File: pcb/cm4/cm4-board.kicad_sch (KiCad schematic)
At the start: 11 parts, among them J201 DF40C-100DS-0.4V_51_, J202 DF40C-100DS-0.4V_51_, U201 SN74LV1T34DBV

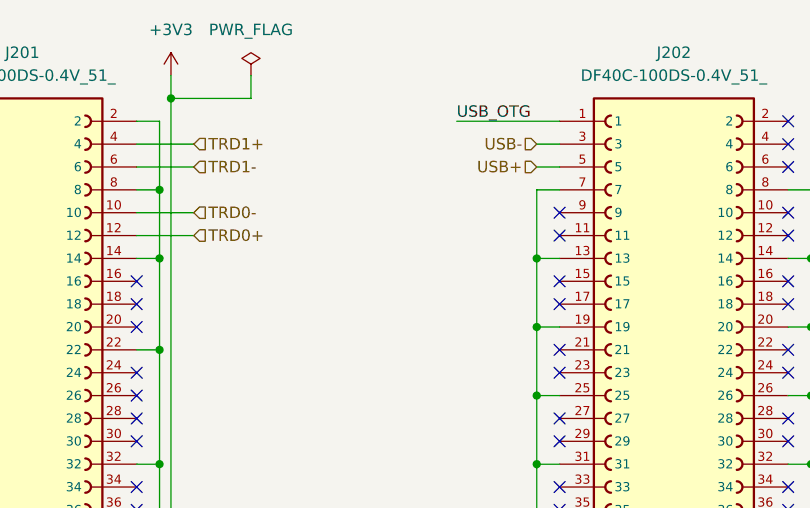
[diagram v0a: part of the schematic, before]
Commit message: add more caps
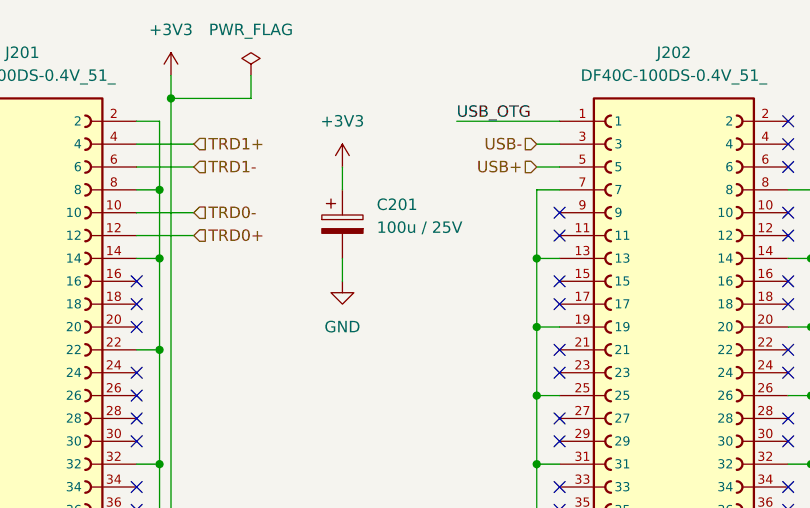
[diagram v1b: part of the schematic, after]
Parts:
- added C201: 100u / 25V, Capacitor_Tantalum_SMD:CP_EIA-7343-43_Kemet-X_Pad2.25x2.55mm_HandSolder, symbol Device:C_Polarized
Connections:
- net +3V3: now also C201.1
- net GND: now also C201.2
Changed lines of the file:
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@@
+	(wire
+		(pts
+			(xy 101.6 36.83) (xy 101.6 39.37)
+		)
+		(stroke
+			(width 0)
+			(type default)
+		)
+	)
 	(wire
 		(pts
@@
 		(pts
 			(xy 50.8 105.41) (xy 53.34 105.41)
+		)
+		(stroke
+			(width 0)
+			(type default)
+		)
+	)
+	(wire
+		(pts
+			(xy 101.6 46.99) (xy 101.6 49.53)
 		)
 		(stroke
@@
 	)
 	(symbol
+		(lib_id "power:GND")
+		(at 101.6 49.53 0)
+		(unit 1)
+		(exclude_from_sim no)
+		(in_bom yes)
+		(on_board yes)
+		(dnp no)
+		(fields_autoplaced yes)
+		(property "Reference" "#PWR0215"
+			(at 101.6 55.88 0)
+			(effects
+				(font
+					(size 1.27 1.27)
+				)
+				(hide yes)
+			)
+		)
+		(property "Value" "GND"
+			(at 101.6 54.61 0)
+			(effects
+				(font
+					(size 1.27 1.27)
+				)
+			)
+		)
+		(property "Footprint" ""
+			(at 101.6 49.53 0)
+			(effects
+				(font
+					(size 1.27 1.27)
+				)
+				(hide yes)
+			)
+		)
+		(property "Datasheet" ""
+			(at 101.6 49.53 0)
+			(effects
+				(font
+					(size 1.27 1.27)
+				)
+				(hide yes)
+			)
+		)
+		(property "Description" "Power symbol creates a global label with name \"GND\" , ground"
+			(at 101.6 49.53 0)
+			(effects
+				(font
+					(size 1.27 1.27)
+				)
+				(hide yes)
+			)
+		)
+		(pin "1"
+		)
+		(instances
+			(project "cm4"
+				(path "/5d20b266-567e-45c6-9e3e-145c2aea1daa/a64f9485-8eaf-45a8-a9d7-21ab5cb8dcb2"
+					(reference "#PWR0215")
+					(unit 1)
+				)
+			)
+		)
+	)
+	(symbol
 		(lib_id "power:+3V3")
 		(at 256.54 107.95 0)
@@
 					(unit 1)
 				)
+			)
+		)
+	)
+	(symbol
+		(lib_id "power:+3V3")
+		(at 101.6 36.83 0)
+		(unit 1)
+		(exclude_from_sim no)
+		(in_bom yes)
+		(on_board yes)
+		(dnp no)
+		(fields_autoplaced yes)
+		(property "Reference" "#PWR0214"
+			(at 101.6 40.64 0)
+			(effects
+				(font
+					(size 1.27 1.27)
+				)
+				(hide yes)
+			)
+		)
+		(property "Value" "+3V3"
+			(at 101.6 31.75 0)
+			(effects
+				(font
+					(size 1.27 1.27)
+				)
+			)
+		)
+		(property "Footprint" ""
+			(at 101.6 36.83 0)
+			(effects
+				(font
+					(size 1.27 1.27)
+				)
+				(hide yes)
+			)
+		)
+		(property "Datasheet" ""
+			(at 101.6 36.83 0)
+			(effects
+				(font
+					(size 1.27 1.27)
+				)
+				(hide yes)
+			)
+		)
+		(property "Description" "Power symbol creates a global label with name \"+3V3\""
+			(at 101.6 36.83 0)
+			(effects
+				(font
+					(size 1.27 1.27)
+				)
+				(hide yes)
+			)
+		)
+		(pin "1"
+		)
+		(instances
+			(project "cm4"
+				(path "/5d20b266-567e-45c6-9e3e-145c2aea1daa/a64f9485-8eaf-45a8-a9d7-21ab5cb8dcb2"
+					(reference "#PWR0214")
+					(unit 1)
+				)
+			)
+		)
+	)
+	(symbol
+		(lib_id "Device:C_Polarized")
+		(at 101.6 43.18 0)
+		(unit 1)
+		(exclude_from_sim no)
+		(in_bom yes)
+		(on_board yes)
+		(dnp no)
+		(fields_autoplaced yes)
+		(property "Reference" "C201"
+			(at 105.41 41.0209 0)
+			(effects
+				(font
+					(size 1.27 1.27)
+				)
+				(justify left)
+			)
+		)
+		(property "Value" "100u / 25V"
+			(at 105.41 43.5609 0)
+			(effects
+				(font
+					(size 1.27 1.27)
+				)
+				(justify left)
+			)
+		)
+		(property "Footprint" "Capacitor_Tantalum_SMD:CP_EIA-7343-43_Kemet-X_Pad2.25x2.55mm_HandSolder"
+			(at 102.5652 46.99 0)
+			(effects
+				(font
+					(size 1.27 1.27)
+				)
+				(hide yes)
+			)
+		)
+		(property "Datasheet" "~"
+			(at 101.6 43.18 0)
+			(effects
+				(font
+					(size 1.27 1.27)
+				)
+				(hide yes)
+			)
+		)
+		(property "Description" "Polarized capacitor"
+			(at 101.6 43.18 0)
+			(effects
+				(font
+					(size 1.27 1.27)
+				)
+				(hide yes)
+			)
+		)
+		(property "LCSC" "C7230"
+			(at 101.6 43.18 0)
+			(effects
+				(font
+					(size 1.27 1.27)
+				)
+				(hide yes)
+			)
+		)
+		(pin "2"
+		)
+		(pin "1"
+		)
+		(instances
+			(project "cm4"
+				(path "/5d20b266-567e-45c6-9e3e-145c2aea1daa/a64f9485-8eaf-45a8-a9d7-21ab5cb8dcb2"
+					(reference "C201")
+					(unit 1)
+				)

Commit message: update lscs fields
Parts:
- D201, D202: LCSC (none) -> C84256
- R201, R204: LCSC (none) -> C17513
- R202, R203, R205, R206: LCSC (none) -> C17520
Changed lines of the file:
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@@
 			)
 		)
-		(property "LCSC" ""
+		(property "LCSC" "C17513"
 			(at 256.54 124.46 0)
 			(effects
@@
 			)
 		)
-		(property "LCSC" ""
+		(property "LCSC" "C17520"
 			(at 224.79 66.04 0)
 			(effects
@@
 			)
 		)
-		(property "LCSC" ""
+		(property "LCSC" "C84256"
 			(at 199.39 118.11 0)
 			(effects
@@
 			)
 		)
-		(property "LCSC" ""
+		(property "LCSC" "C17520"
 			(at 177.8 64.77 0)
 			(effects
@@
 			)
 		)
-		(property "LCSC" ""
+		(property "LCSC" "C17520"
 			(at 190.5 64.77 0)
 			(effects
@@
 			)
 		)
-		(property "LCSC" ""
+		(property "LCSC" "C17513"
 			(at 199.39 128.27 0)
 			(effects
@@
 			)
 		)
-		(property "LCSC" ""
+		(property "LCSC" "C17520"
 			(at 224.79 53.34 0)
 			(effects
@@
 			)
 		)
-		(property "LCSC" ""
+		(property "LCSC" "C84256"
 			(at 256.54 114.3 0)
 			(effects

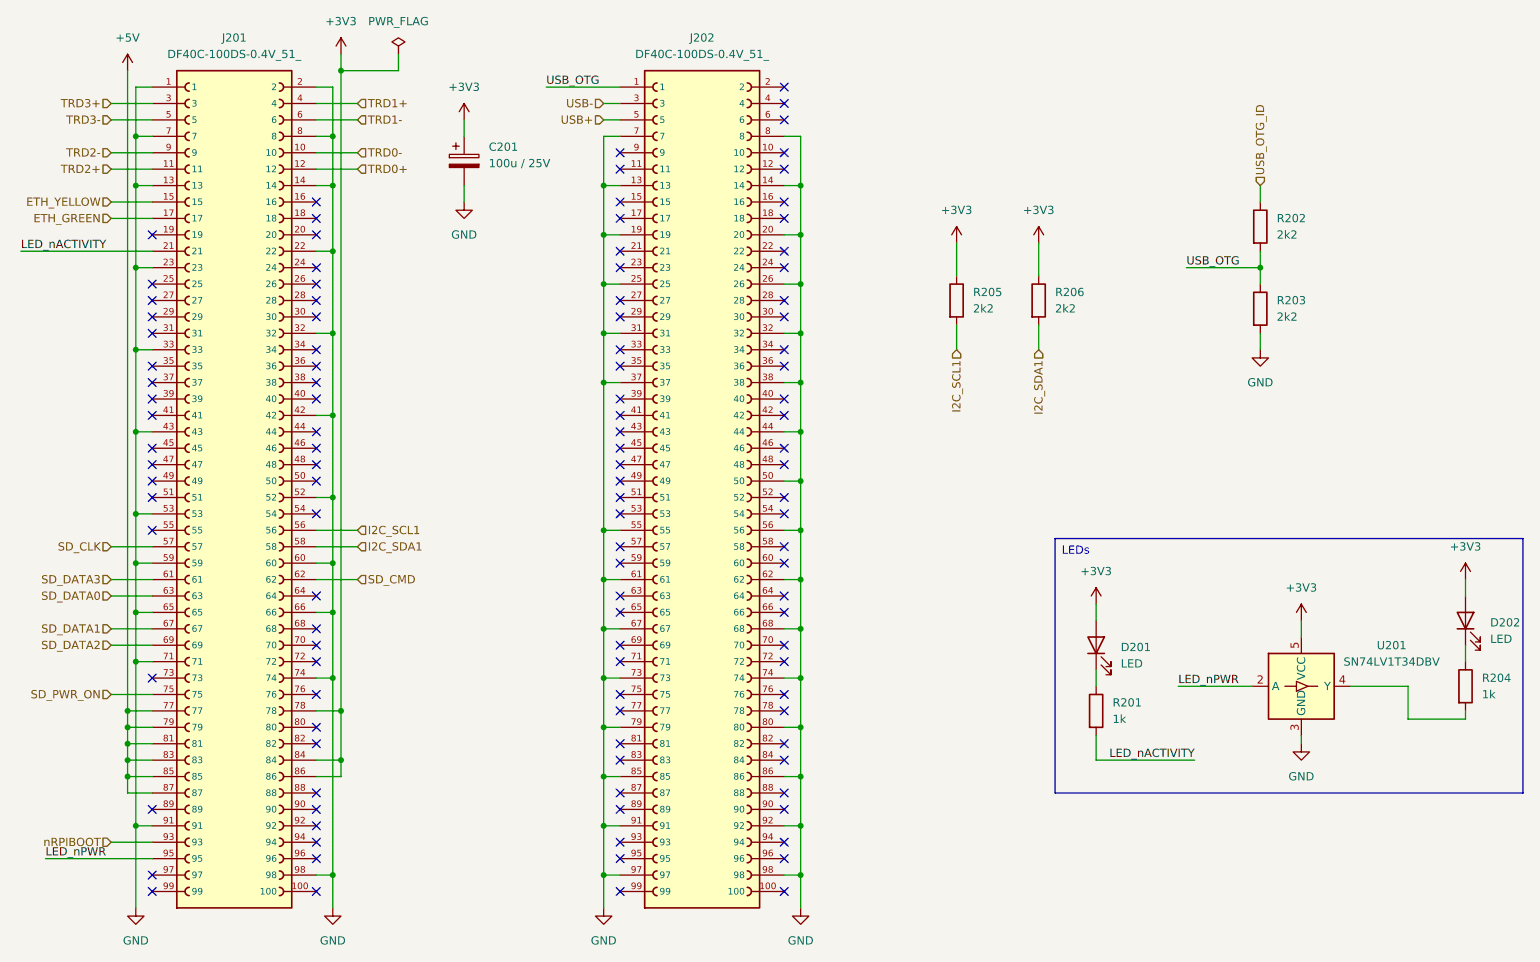
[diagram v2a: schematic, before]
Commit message: upgrade to kicad 9.0.0
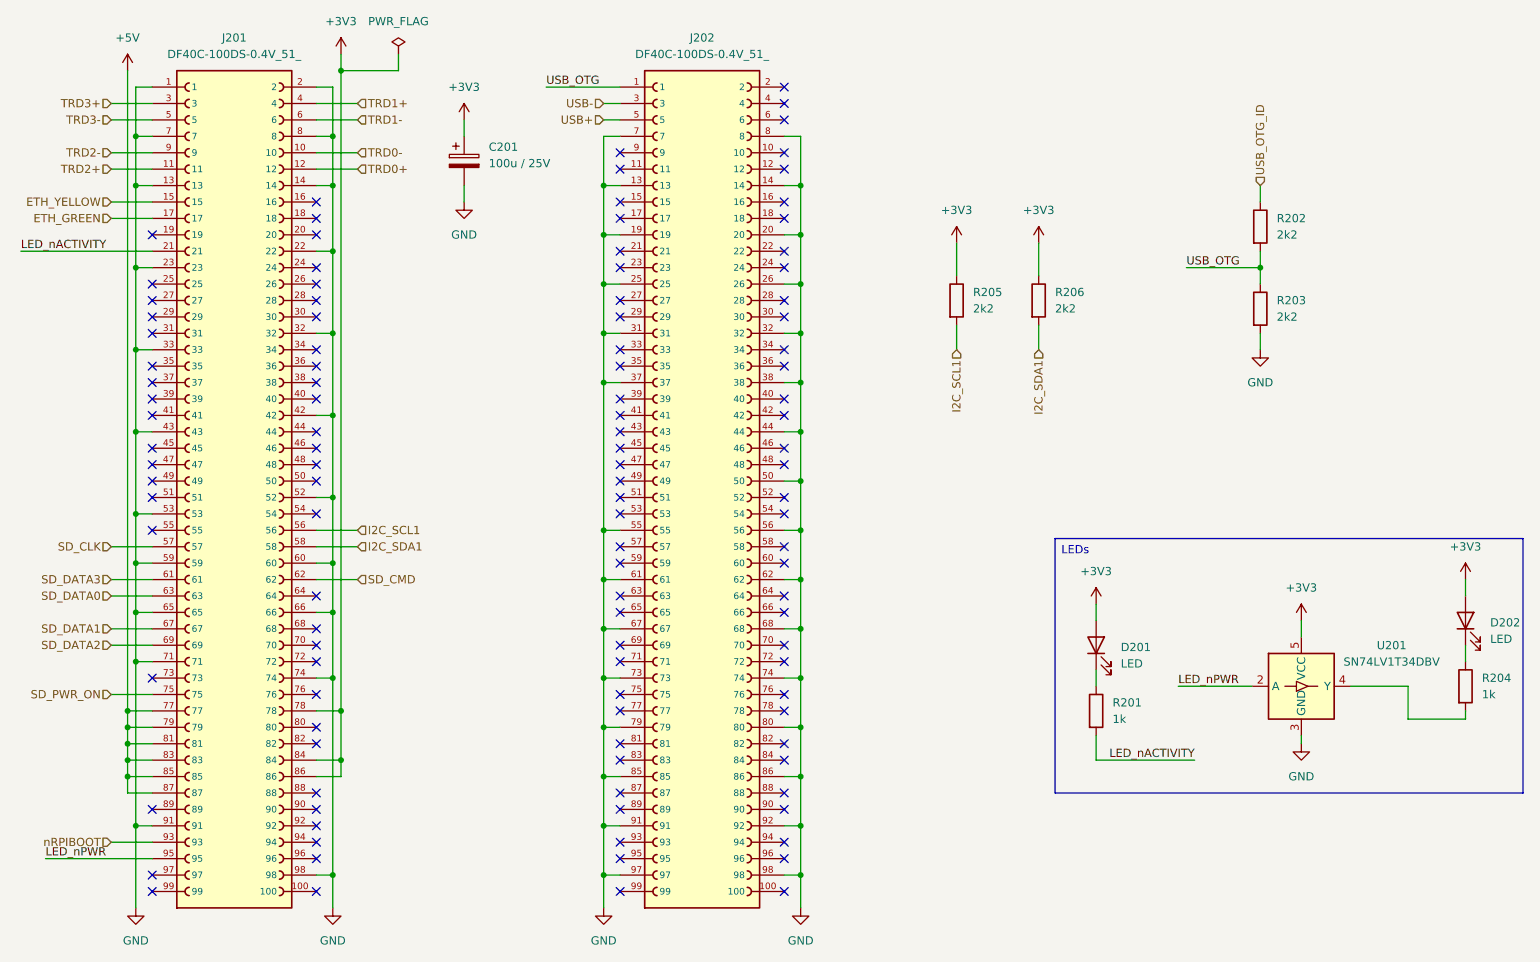
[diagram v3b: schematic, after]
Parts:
- J201, J202: Availability (none) -> In Stock; Check_prices (none) -> https://www.snapeda.com/parts/DF40C-100DS-0.4V(51)/Hirose/v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; Description_1 (none) -> 100 Position Connector Receptacle, Center Strip Contacts Su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; MANUFACTURER (none) -> Hirose; MAXIMUM_PACKAGE_HEIGHT (none) -> 1.65mm; MF (none) -> Hirose; MP (none) -> DF40C-100DS-0.4V(51); PARTREV (none) -> Oct.1.2023; Package (none) -> None; Price (none) -> None; STANDARD (none) -> Manufacturer Recommendations; SnapEDA_Link (none) -> https://www.snapeda.com/parts/DF40C-100DS-0.4V(51)/Hirose/v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
